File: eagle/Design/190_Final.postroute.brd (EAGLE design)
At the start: 160 x 100 mm, 29 parts, among them U1_0_BRAIN ADAFRUIT-PRO-TRINKET-5V-BOB, U1_6_CASTER CASTERADAFRUIT-3/4IN, U1_7_CASTER_2 CASTERADAFRUIT-3/4IN

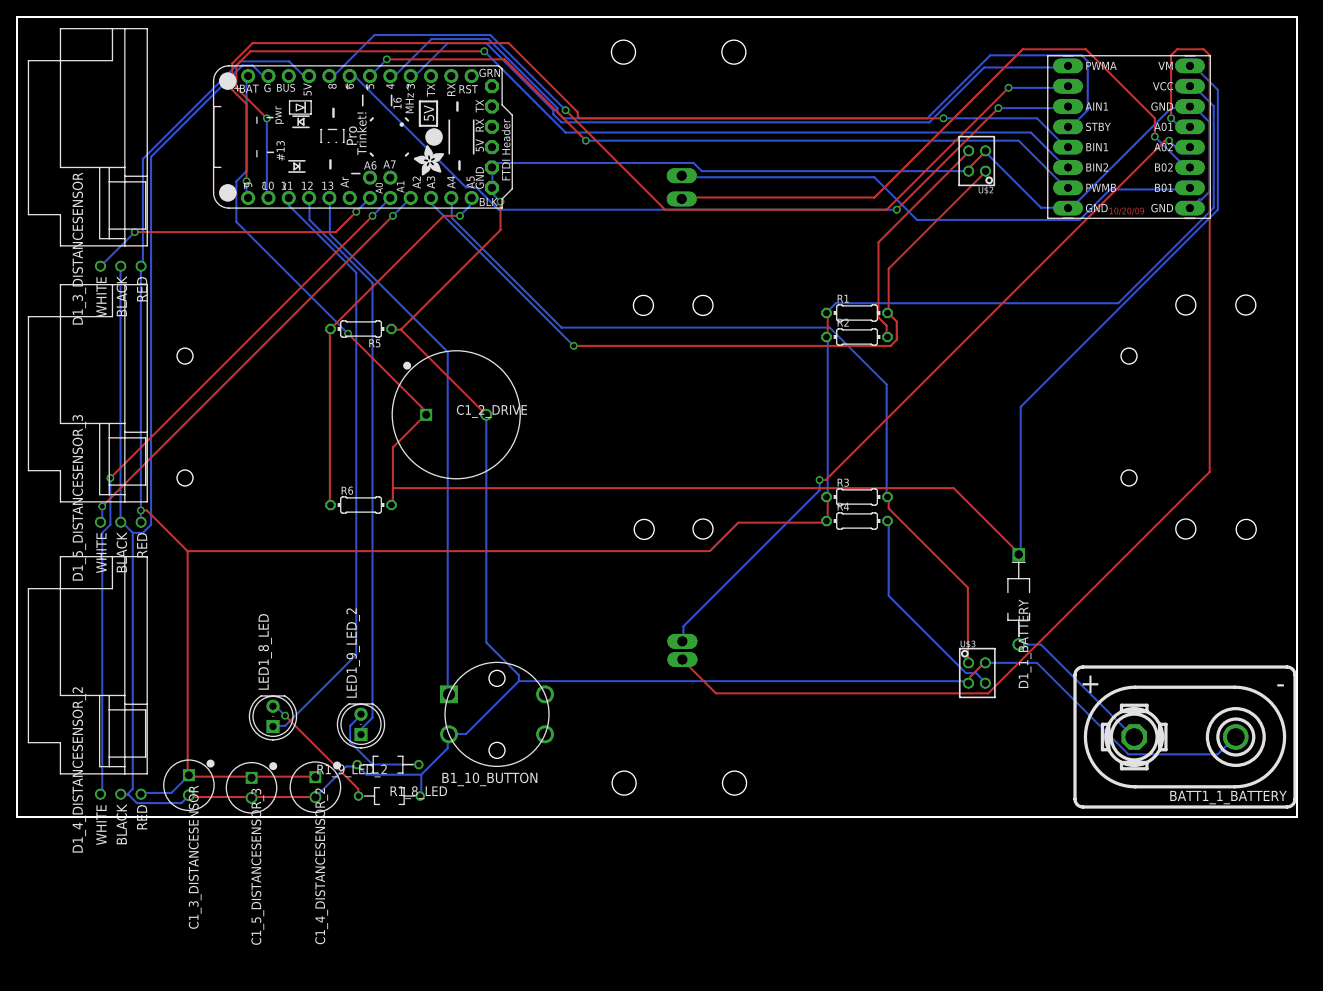
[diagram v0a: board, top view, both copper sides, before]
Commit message: Updated make files/lpkf board
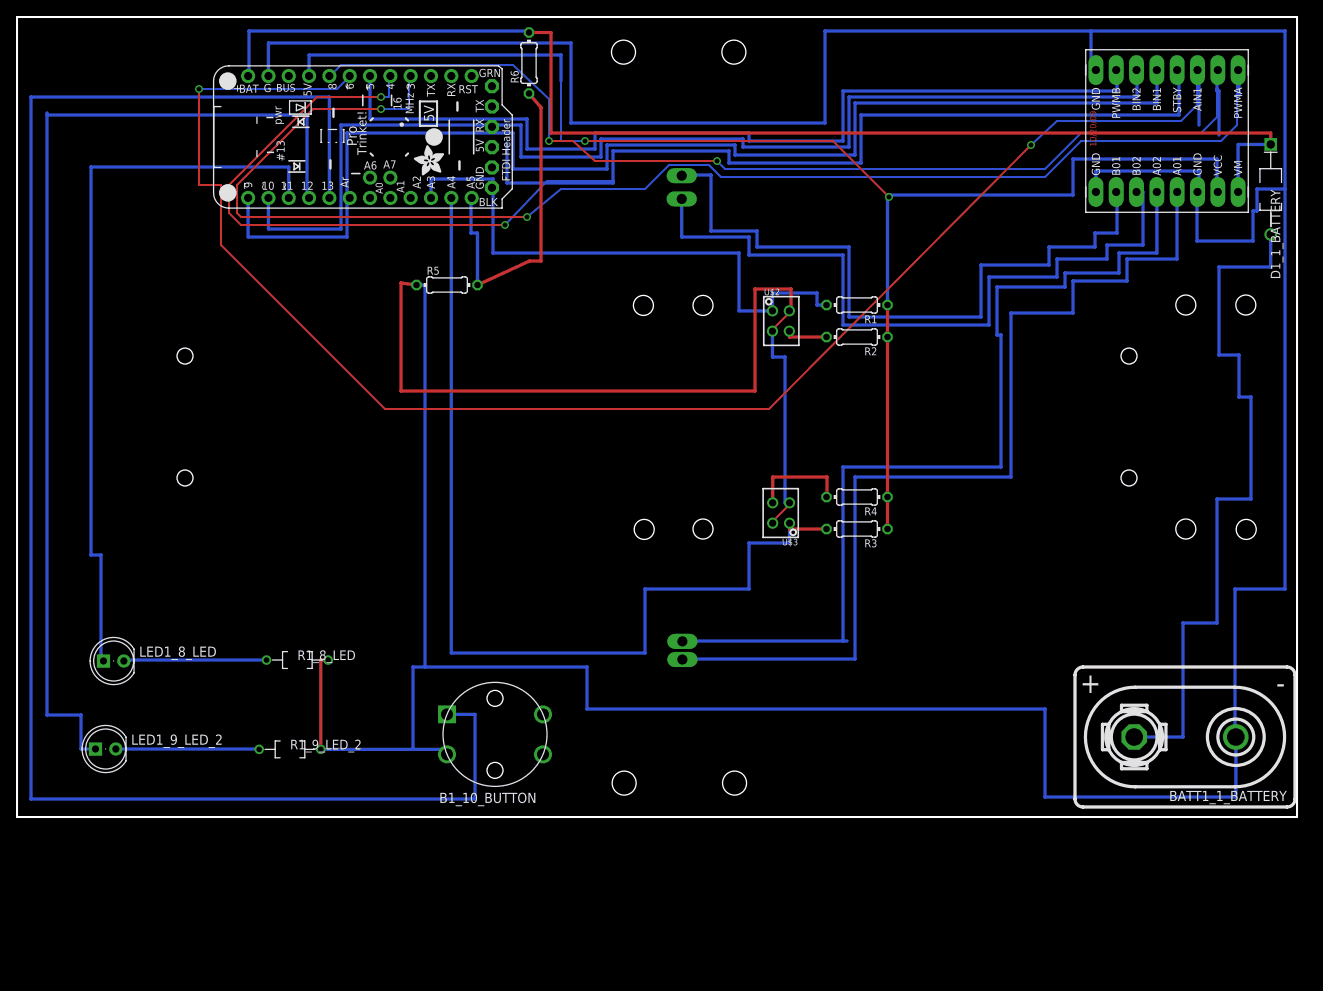
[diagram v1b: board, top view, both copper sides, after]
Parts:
- removed C1_2_DRIVE: 3300uF, KoalaBuild:CAPPRD750W80D1600H2200P
- removed C1_3_DISTANCESENSOR, C1_4_DISTANCESENSOR_2, C1_5_DISTANCESENSOR_3: 100uF, KoalaBuild:CAPPRD250W80D630H1220P
- removed D1_3_DISTANCESENSOR, D1_4_DISTANCESENSOR_2, D1_5_DISTANCESENSOR_3: ANALOG_DISTANCE_SENSOR-GLUE, Components:ANALOG_DISTANCE_SENSOR_GLUE_MOUNT
- moved D1_1_BATTERY 60.2 mm to (76.7, 28.4)
- moved R6 59.1 mm to (-16.0, 44.2), turned to 90 degrees
- moved LED1_9_LED_2 32.1 mm to (-68.9, -41.5), turned to 0 degrees
- moved U$2 31.6 mm to (15.5, 12.0), turned to 0 degrees
- moved U$3 31.6 mm to (15.5, -12.0), turned to 180 degrees
- moved LED1_8_LED 21.1 mm to (-67.9, -30.5), turned to 0 degrees
- moved R1_8_LED 20.5 mm to (-45.0, -30.4)
- moved R1_9_LED_2 12.4 mm to (-45.9, -41.5), turned to 0 degrees
- moved R5 12.1 mm to (-26.2, 16.5), turned to 0 degrees
- moved DRVR_2_DRIVE 4.81 mm to (63.8, 35.8), turned to 270 degrees
- moved R3 4.00 mm to (25.0, -14.0), turned to 180 degrees
- moved R4 3.00 mm to (25.0, -10.0), turned to 180 degrees
- moved B1_10_BUTTON 2.51 mm to (-20.2, -39.7)
- moved R1 1.00 mm to (25.0, 14.0), turned to 180 degrees
- turned R2 to 180 degrees
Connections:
- net VBUS_0_BRAIN renamed DISCONNECTED_3
- new net DISCONNECTED: U1_0_BRAIN.GND
- new net DISCONNECTED_2: U1_0_BRAIN.GND1
- net +5V_0_BRAIN: no longer C1_3_DISTANCESENSOR.1, C1_4_DISTANCESENSOR_2.1, C1_5_DISTANCESENSOR_3.1, D1_3_DISTANCESENSOR.VCC, D1_4_DISTANCESENSOR_2.VCC, D1_5_DISTANCESENSOR_3.VCC
- net A0_0_BRAIN: no longer D1_3_DISTANCESENSOR.VO
- net A1_0_BRAIN: no longer D1_4_DISTANCESENSOR_2.VO
- net A2_0_BRAIN: no longer D1_5_DISTANCESENSOR_3.VO
- net GND_0_BRAIN: no longer C1_2_DRIVE.2, C1_3_DISTANCESENSOR.2, C1_4_DISTANCESENSOR_2.2, C1_5_DISTANCESENSOR_3.2, D1_3_DISTANCESENSOR.GND, D1_4_DISTANCESENSOR_2.GND, D1_5_DISTANCESENSOR_3.GND, U1_0_BRAIN.GND, U1_0_BRAIN.GND1
- net POS_1_BATTERY: no longer C1_2_DRIVE.1
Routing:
- net D13_0_BRAIN: track 68.2 -> 208.1 mm
- net GND_0_BRAIN: track 484.3 -> 620.5 mm, vias 1 -> 0
- net +5V_0_BRAIN: track 309.7 -> 180.6 mm, vias 1 -> 2
- net D6_0_BRAIN: track 102.2 -> 199.4 mm
- net A1_0_BRAIN: track 89.6 -> 0.00 mm, vias 2 -> 0
- net D3_0_BRAIN: track 91.3 -> 174.6 mm, vias 0 -> 2
- net D4_0_BRAIN: track 106.7 -> 188.1 mm, vias 0 -> 2
- net N$1_1_BATTERY: track 19.2 -> 88.5 mm
- net POS_1_BATTERY: track 220.9 -> 157.6 mm, vias 1 -> 0
- net D12_0_BRAIN: track 71.0 -> 128.7 mm
- net A2_0_BRAIN: track 56.6 -> 0.00 mm, vias 2 -> 0
- net A0_0_BRAIN: track 37.2 -> 0.00 mm, vias 2 -> 0
- net A01_2_DRIVE: track 147.3 -> 120.3 mm, vias 1 -> 0
- net A02_2_DRIVE: track 91.5 -> 117.0 mm, vias 2 -> 0
- net D8_0_BRAIN: track 110.0 -> 134.5 mm
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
